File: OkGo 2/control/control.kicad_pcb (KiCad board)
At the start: 2 copper layers, 92.2 x 64.5 mm, 72 parts, among them M3_MOUNT VAL**, P102 KEYSW, P105 BATT, P106 ARM_LED, P108 SMA, P110 POWER_SW, P111 SERIAL, P201 CH1, P202 CH2, P205 CH3, P206 CH4, Q201 BSS138BK, Q202 BSS138BK, Q203 BSS138BK, Q204 BSS138BK, U101 SWD, U102 STM32F071CBT6, U103 MEJ2S0305SC, U105 RFM95W, U106 LCD_HD44780, U107 ADP3335, Y101 8MHz

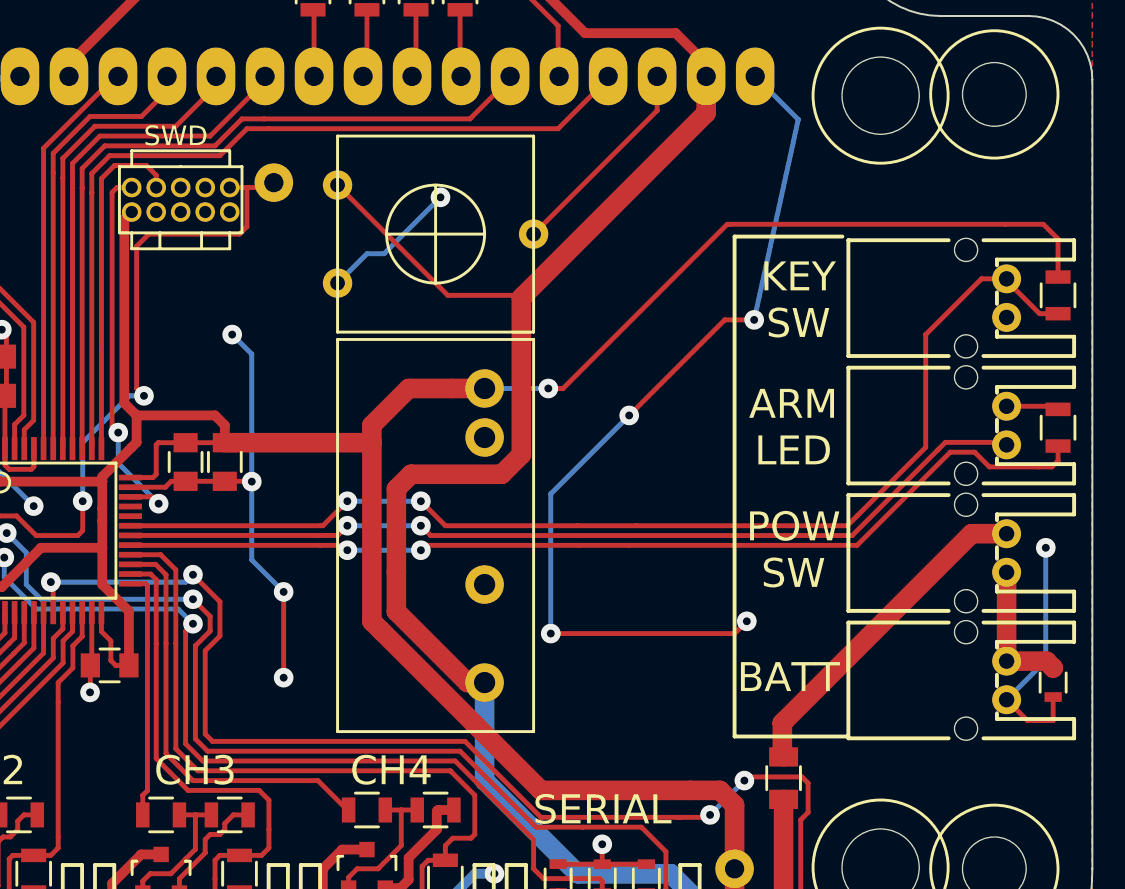
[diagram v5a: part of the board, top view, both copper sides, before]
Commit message: Added LEDs to control
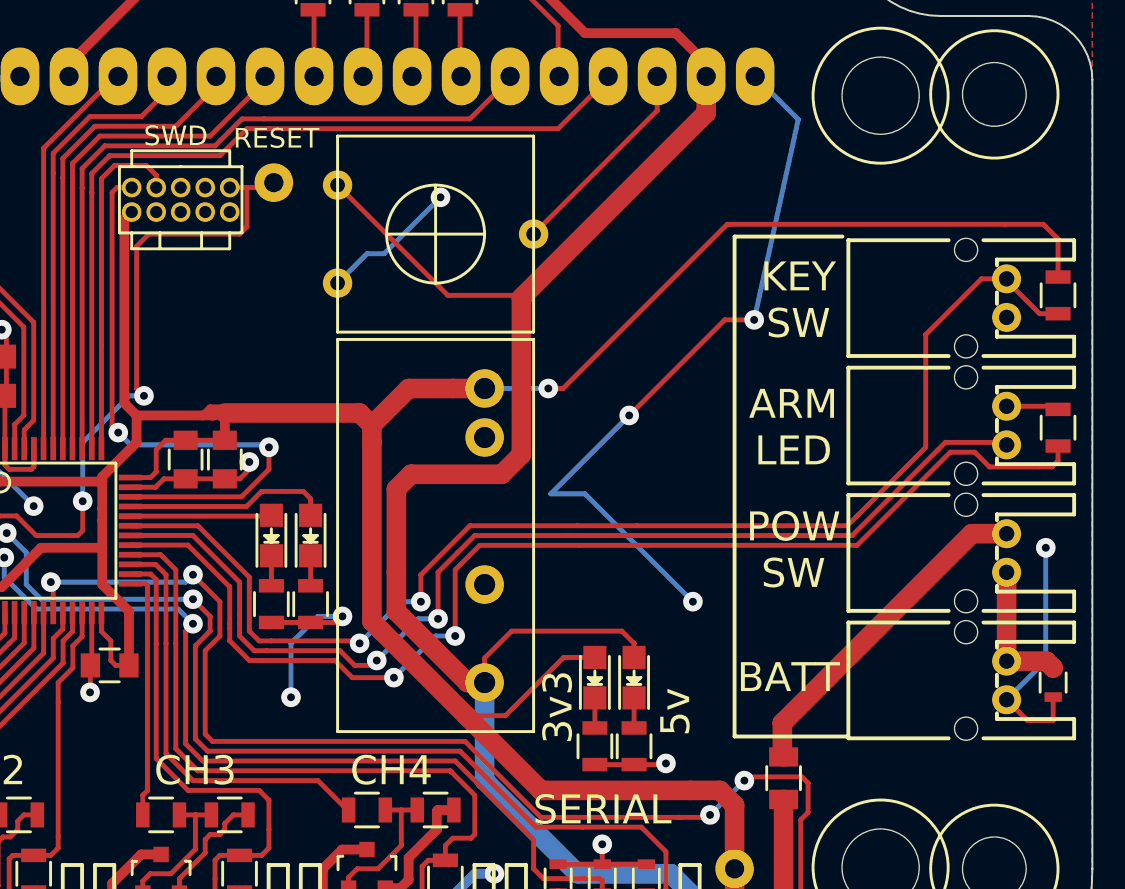
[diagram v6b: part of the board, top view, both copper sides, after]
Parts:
- added D107: RED, LEDs:LED-0805, F.Cu at (199.0, 110.5)
- added D108: GREEN, LEDs:LED-0805, F.Cu at (184.3, 103.1)
- added D109: eYELLOW, LEDs:LED-0805, F.Cu at (182.2, 103.1)
- added D110: RED, LEDs:LED-0805, F.Cu at (201.0, 110.5)
- added R104: R_Small, Resistors_SMD:R_0805, F.Cu at (199.0, 114.0)
- added R111: R, Resistors_SMD:R_0805, F.Cu at (184.3, 106.7)
- added R112: R, Resistors_SMD:R_0805, F.Cu at (182.2, 106.7)
- added R113: R, Resistors_SMD:R_0805, F.Cu at (201.0, 114.0)
- TP101: value RESET -> nRST
- moved C106 0.13 mm to (177.8, 99.2)
- moved C107 0.13 mm to (179.8, 99.2)
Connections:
- U102 pad 32: (no net) -> Net-(D109-Pad2)
- U102 pad 33: (no net) -> Net-(D108-Pad2)
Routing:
- net GND: track 420.9 -> 407.8 mm, vias 42 -> 41
- net /SWDIO: track 19.9 -> 30.7 mm
- net Net-(D108-Pad2): track 0.00 -> 10.7 mm
- net +5V: track 184.2 -> 194.8 mm
- net +3V3: track 354.5 -> 364.1 mm
- net /ARM_LED: track 51.5 -> 60.7 mm
- net /DISARM_LED: track 47.8 -> 56.1 mm
- net Net-(D109-Pad2): track 0.00 -> 7.33 mm
- net /ARM_SW: track 59.1 -> 65.6 mm
- net Net-(D110-Pad1): track 0.00 -> 1.56 mm
- net Net-(D109-Pad1): track 0.00 -> 1.56 mm
- net Net-(D108-Pad1): track 0.00 -> 1.56 mm
- net Net-(D107-Pad1): track 0.00 -> 1.56 mm
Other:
- board text added: "3v3"
- board text added: "5v"
- board text added: "RESET"
